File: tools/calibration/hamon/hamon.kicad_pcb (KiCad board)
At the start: 2 copper layers, 35 x 30 mm, 11 parts, among them SW1 SW_DPST

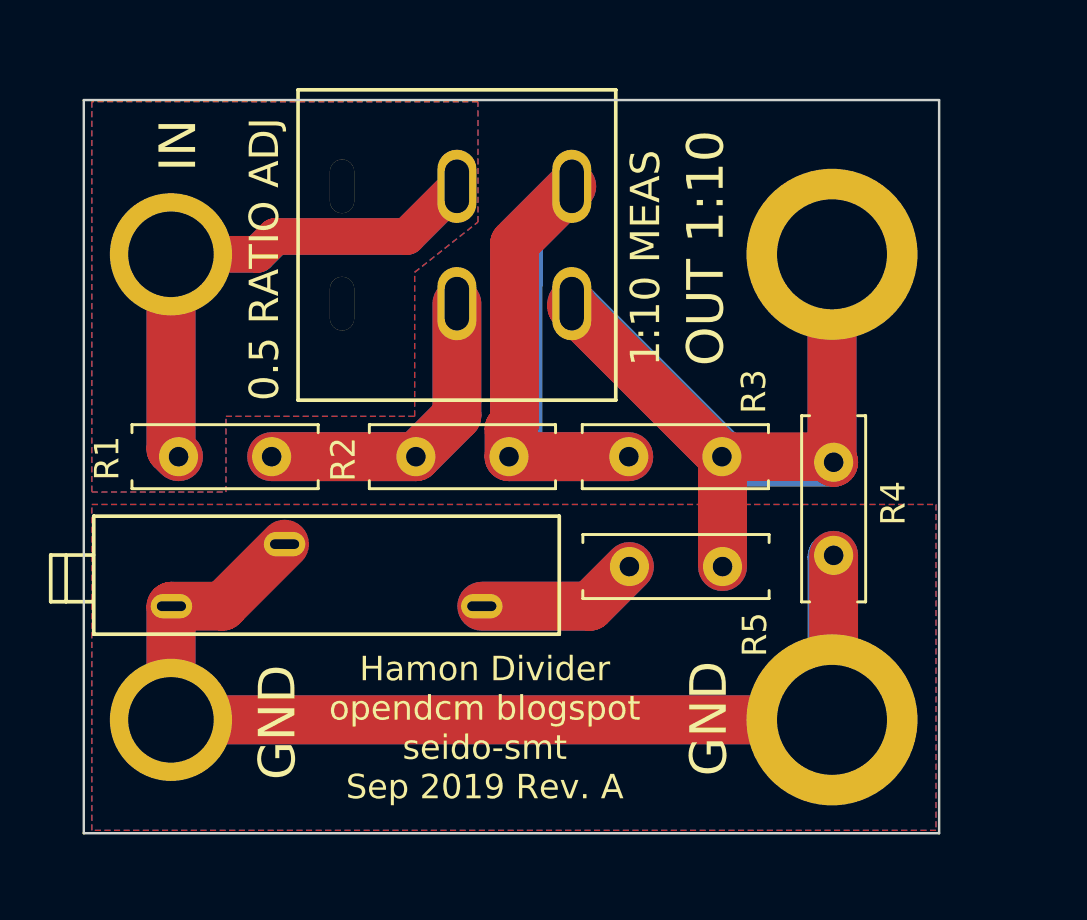
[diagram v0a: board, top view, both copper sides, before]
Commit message: Added updated hamon divider PCB
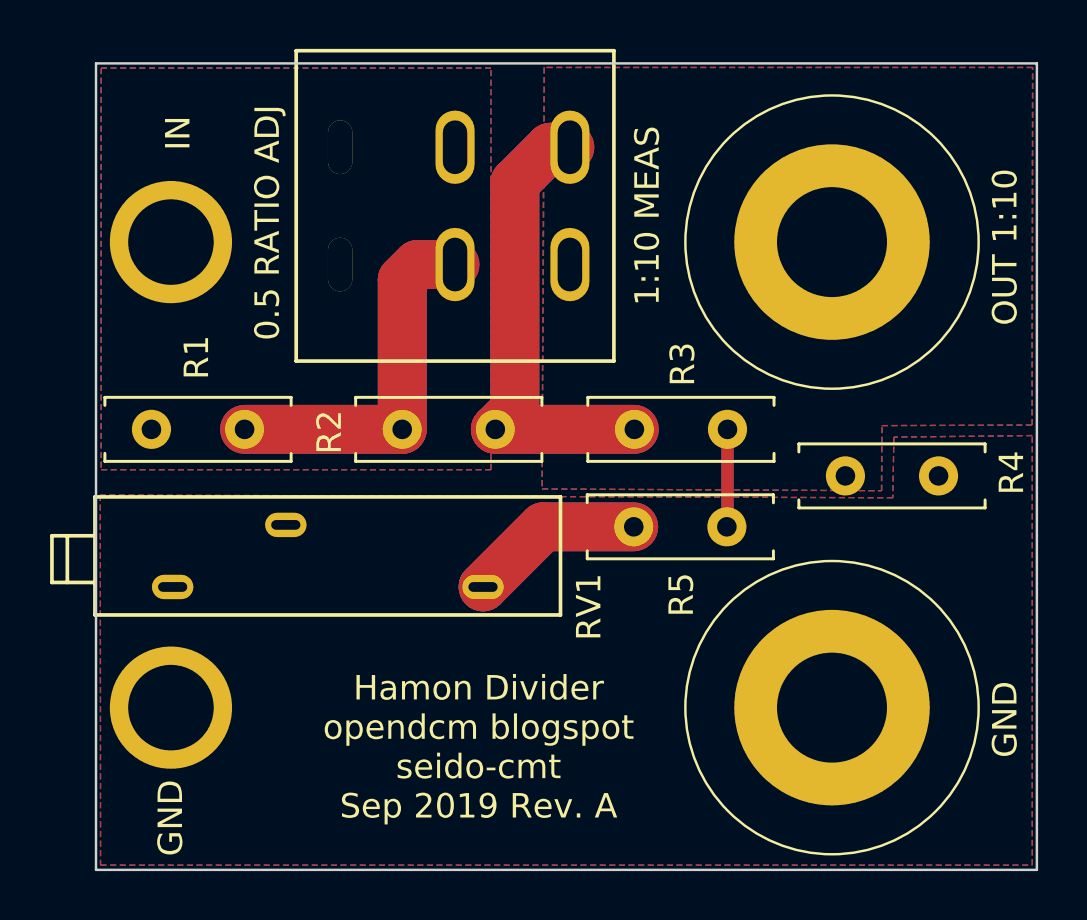
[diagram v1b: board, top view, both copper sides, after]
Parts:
- moved R4 2.74 mm to (133.1, 65.4), turned to 0 degrees
- moved R5 1.64 mm to (124.4, 67.5)
- moved SW1 1.60 mm to (121.7, 48.0)
- moved R1 1.57 mm to (104.7, 63.5)
- moved R2 1.25 mm to (114.9, 63.5)
- moved R3 1.14 mm to (124.4, 63.5)
- moved RV1 0.79 mm to (119.5, 71.1)
- moved H1 0.50 mm to (103.6, 55.8)
- moved H2 0.50 mm to (103.6, 74.9)
- moved H3 0.50 mm to (130.6, 55.8), turned to 90 degrees
- moved H4 0.50 mm to (130.6, 74.9)
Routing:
- net GND: track 82.6 -> 0.00 mm
- net OUT: track 53.0 -> 8.00 mm
- net IN: track 42.5 -> 2.26 mm
- net Net-(R1-Pad2): track 25.7 -> 30.0 mm
- net Net-(R2-Pad2): track 34.1 -> 37.9 mm
- net Net-(R5-Pad2): track 13.4 -> 14.4 mm
- added copper zone on B.Cu, net OUT
- added copper zone on F.Cu, net OUT
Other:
- board size 35 x 30 mm -> 38.5 x 33 mm
- board text added: "Hamon Divider opendcm blogspot seido-cmt Sep 2019 Rev. A"
- board text removed: "Hamon Divider opendcm blogspot seido-smt Sep 2019 Rev. A"
